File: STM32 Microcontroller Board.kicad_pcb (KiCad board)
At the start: 4 copper layers, 74.8 x 98.3 mm, 182 parts, among them J1 F407 SWD, J10 USB_B_Micro, J2 GPIO, J3 Conn_01x02_Pin, J4 F103 SWD, J5 USB_B_Micro, J6 Ethernet, J7 12V IN, J8 12V RGB LED, J9 Relay IO, Q1 PMOS, Q2 NMOS, Q3 NMOS, Q4 NMOS, SW1 SW_Push, SW2 SW_Push, SW3 SW_Push, SW4 SW_Push, SW5 SW_Push, SW6 SW_Push, U1 STM32F407VGTx, U2 MCP1825S-3302E/EB, U3 STM32F103C8T6, U4 USBLC6-2, U5 DP83826IRHBR, U6 TLV9001TIDCKR, U7 ULN2803CDWR, U8 USBLC6-2, Y1 8MHz, Y2 25MHz

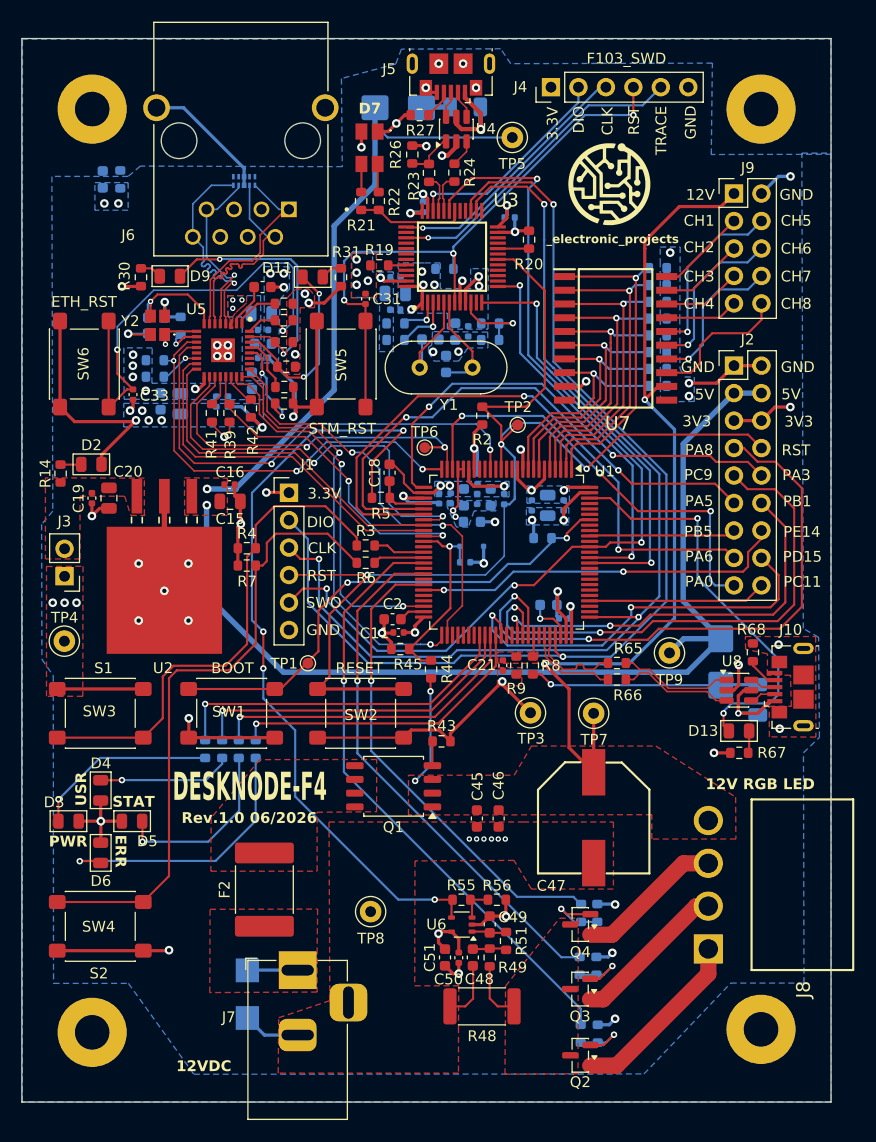
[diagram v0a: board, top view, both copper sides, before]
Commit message: Alternate MPNs added
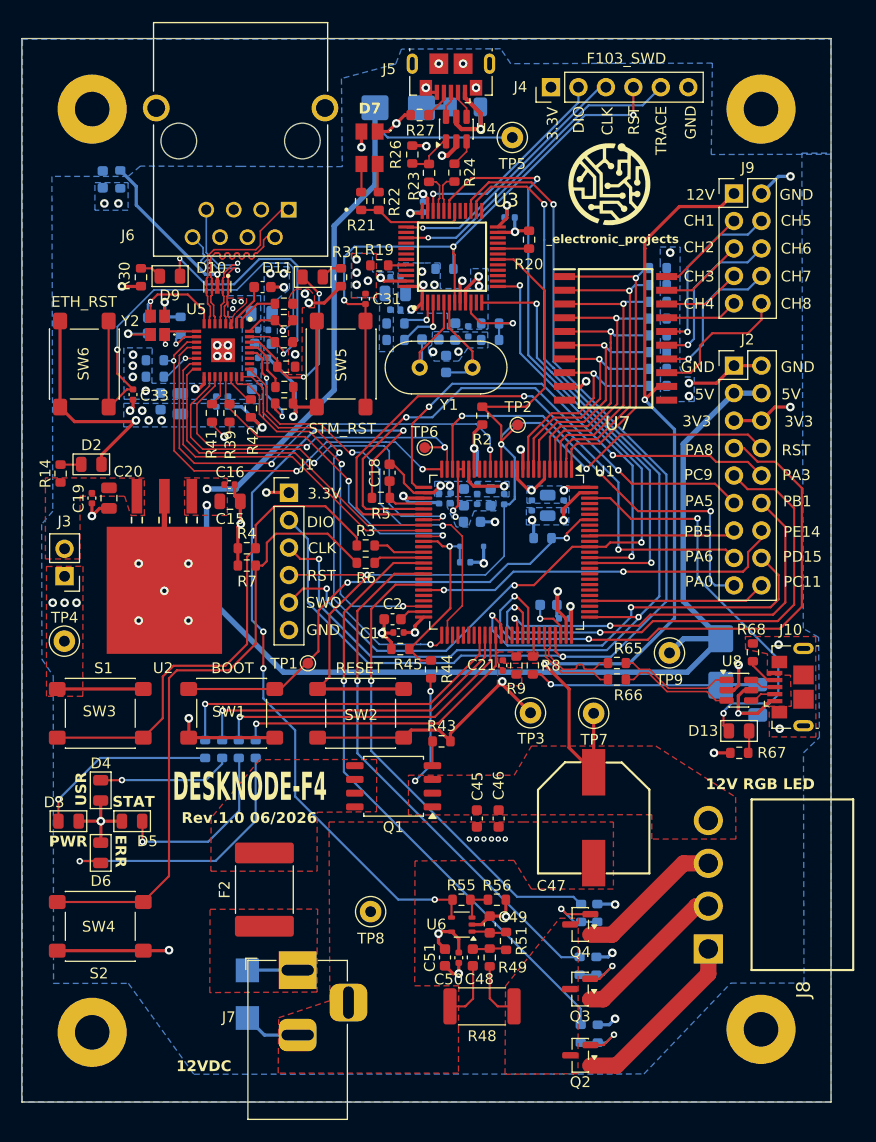
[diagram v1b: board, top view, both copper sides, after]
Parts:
- D10: moved to F.Cu
- moved D10 10.1 mm to (119.2, 65.3)
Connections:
- D10 pad 1: /Ethernet PHY/TD_P -> /Ethernet PHY/RD_N
- D10 pad 10: unconnected-(D10-NC_4-Pad10) -> /Ethernet PHY/RD_N
- D10 pad 2: /Ethernet PHY/TD_N -> /Ethernet PHY/RD_P
- D10 pad 4: /Ethernet PHY/RD_P -> /Ethernet PHY/TD_N
- D10 pad 5: /Ethernet PHY/RD_N -> /Ethernet PHY/TD_P
- D10 pad 6: unconnected-(D10-NC_1-Pad6) -> /Ethernet PHY/TD_P
- D10 pad 7: unconnected-(D10-NC_2-Pad7) -> /Ethernet PHY/TD_N
- D10 pad 9: unconnected-(D10-NC_3-Pad9) -> /Ethernet PHY/RD_P
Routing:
- net /Ethernet PHY/RD_N: track 20.4 -> 13.9 mm
- net /Ethernet PHY/TD_N: track 20.2 -> 16.4 mm
- net Earth: track 12.0 -> 15.5 mm, vias 0 -> 1
- net /Ethernet PHY/RD_P: track 17.0 -> 14.0 mm
- net /Ethernet PHY/LED1: track 24.7 -> 27.6 mm
- net /Ethernet PHY/TD_P: track 19.1 -> 16.5 mm
- net /Debugger/STM_RST: track 57.2 -> 58.3 mm

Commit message: SV's comments
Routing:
- net Net-(U1-VDDA): track 4.51 -> 5.18 mm
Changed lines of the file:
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@@
 		(tags "LED")
 		(property "Reference" "D9"
-			(at 0.0125 -1.775 0)
+			(at -0.7125 -1.875 0)
 			(layer "F.SilkS")
 			(effects
@@
 	)
 	(segment
+		(start 141.2 86.625)
+		(end 141.2 86.275)
+		(width 0.2)
+		(layer "F.Cu")
+		(net 4)
+	)
+	(segment
+		(start 141.2 86.275)
+		(end 140.975 86.05)
+		(width 0.2)
+		(layer "F.Cu")
+		(net 4)
+	)
+	(segment
 		(start 141.425 85.6)
 		(end 140.975 86.05)
@@
 	)
 	(via
-		(at 158.7 75.8)
+		(at 137.4648 111.0488)
 		(size 0.6)
 		(drill 0.3)
@@
 	)
 	(via
-		(at 137.4648 111.0488)
+		(at 158.7 75.8)
 		(size 0.6)
 		(drill 0.3)
 		(layers "F.Cu" "B.Cu")
-		(free yes)
 		(net 20)
 	)
@@
 		(target_length 16.5)
 		(target_length_max 16.6)
-		(target_length_min 16.4)
+		(target_length_min 16.399999)
 		(target_skew 0)
 		(target_skew_max 0.1)

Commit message: All comments addressed
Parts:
- added D15: SMBJ15A, footprints:SMBJ15A, B.Cu at (159.1, 114.7)
- added D16: SMF15A, Diode_SMD:D_SMF, B.Cu at (160.3, 118.7)
- added D17: SMF15A, Diode_SMD:D_SMF, B.Cu at (160.3, 122.6)
- added D18: SMF15A, Diode_SMD:D_SMF, B.Cu at (160.3, 126.7)
- added R69: 0R, Resistor_SMD:R_0603_1608Metric, B.Cu at (160.6, 76.1)
- added R70: 0R, Resistor_SMD:R_0603_1608Metric, B.Cu at (161.7, 101.0)
- added R71: 0R, Resistor_SMD:R_0603_1608Metric, B.Cu at (133.7, 54.1)
- C32: footprint Capacitor_SMD:C_0603_1608Metric -> Capacitor_SMD:C_1206_3216Metric
- D10: value ESD7104MUTAG -> SP1004U-ULC-04UTG
- TP3, TP8: value GND -> TestPoint
- TP4: value 3V3 -> TestPoint
- TP5, TP9: value 5V -> TestPoint
- TP7: value 12V -> TestPoint
- moved C23 5.06 mm to (145.3, 73.1), turned to 180 degrees
- moved C22 4.48 mm to (135.2, 72.8), turned to 0 degrees
- moved R26 1.13 mm to (138.3, 52.9), turned to 0 degrees
- moved TP9 0.93 mm to (161.7, 98.6)
- moved R24 0.56 mm to (140.6, 55.1)
- moved C50 0.49 mm to (141.5, 126.9)
- moved U6 0.49 mm to (141.7, 123.8)
- moved C48 0.49 mm to (142.8, 126.9)
- moved C49 0.49 mm to (144.3, 123.8)
- moved R49 0.49 mm to (144.3, 126.9)
- moved C51 0.49 mm to (140.2, 126.9)
- moved R51 0.49 mm to (145.8, 125.4)
- moved R55 0.49 mm to (141.7, 121.5)
- moved R56 0.49 mm to (145.0, 121.5)
- moved R23 0.43 mm to (139.1, 55.1)
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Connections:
- D14 pad 1: +5V -> Net-(D14-K)
- D8 pad 1: +5V -> Net-(D8-K)
- J9 pad 1: +12V -> /AC PWR ctrl & USB FS/V+
- Q1 pad 1: +12V -> Net-(Q1-G)
- Q1 pad 3: +12V -> Net-(Q1-D)
- U7 pad 12: +12V -> /AC PWR ctrl & USB FS/V+
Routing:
- net GND: track 200.2 -> 72.2 mm, vias 71 -> 85
- net +12V: track 90.0 -> 59.1 mm, vias 4 -> 3
- net /AC PWR ctrl & USB FS/V+: track 0.00 -> 28.5 mm, vias 0 -> 1
- net /Ethernet PHY/RD_N: track 13.9 -> 31.8 mm, vias 1 -> 0
- net /Ethernet PHY/RD_P: track 14.0 -> 31.4 mm, vias 1 -> 0
- net +5V: track 153.1 -> 136.9 mm
- net +3.3V: track 99.2 -> 89.5 mm, vias 36 -> 33
- net Net-(D14-K): track 0.00 -> 4.26 mm
- net Net-(D8-K): track 0.00 -> 3.88 mm
- net /LED Driver/B_LED: track 13.6 -> 16.5 mm
- net /LED Driver/G_LED: track 14.5 -> 17.4 mm
- net /LED Driver/R_LED: track 16.7 -> 19.1 mm
- net Net-(R23-Pad1): track 4.45 -> 3.13 mm
- net Net-(U3-PD1-OSC_OUT): track 9.52 -> 10.2 mm
- net /Debugger/USB_N: track 3.62 -> 2.91 mm
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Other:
- board text added: "Rev.1.0 07/2026"
- board text added: "V+"
- board text removed: "12V"
- board text removed: "Rev.1.0 06/2026"
